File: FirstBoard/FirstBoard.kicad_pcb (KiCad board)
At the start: 2 copper layers, 82 x 122.1 mm, 26 parts, among them J0 Battery, J1 MPU0, J10 MPU9, J11 MPU10, J12 MPU11, J13 MPU12, J15 SD_CARD, J2 MPU1, J3 MPU3, J4 MPU3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

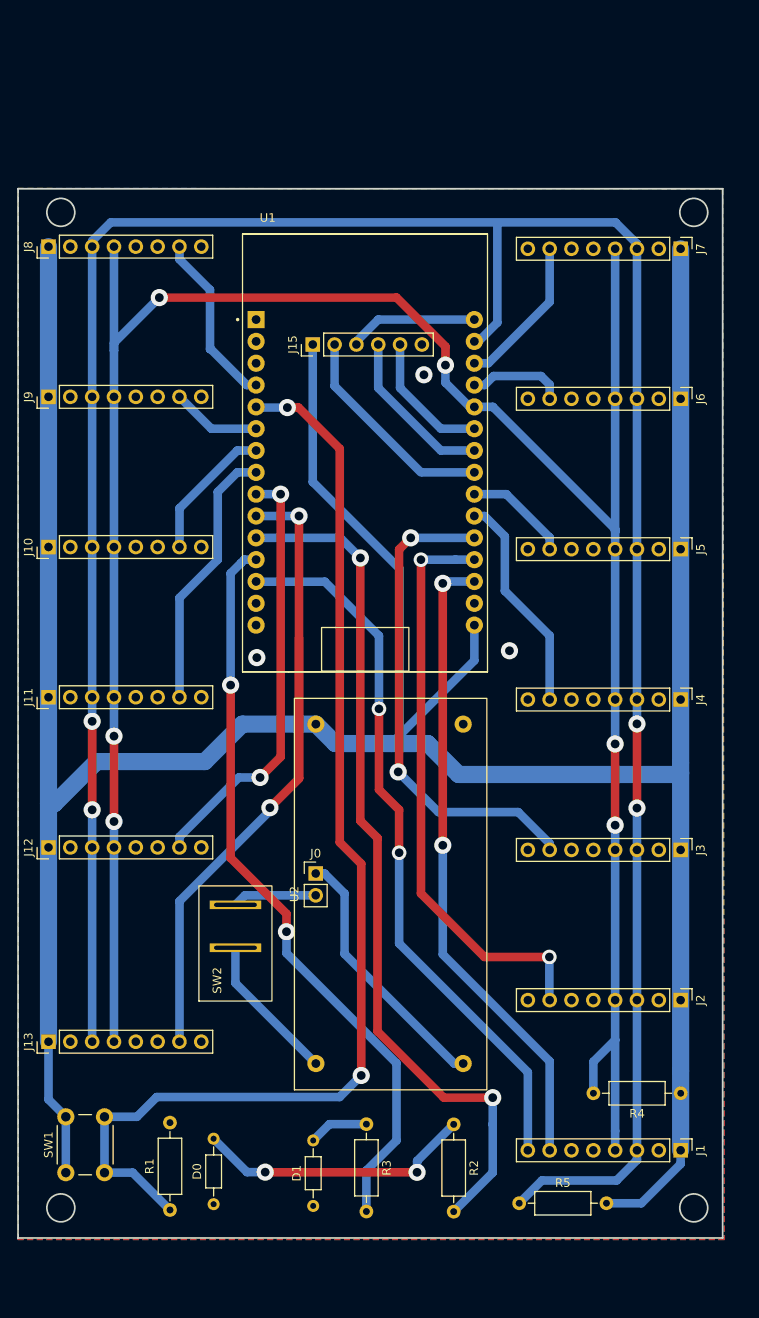
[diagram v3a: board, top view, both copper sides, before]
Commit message: Adjusted holes
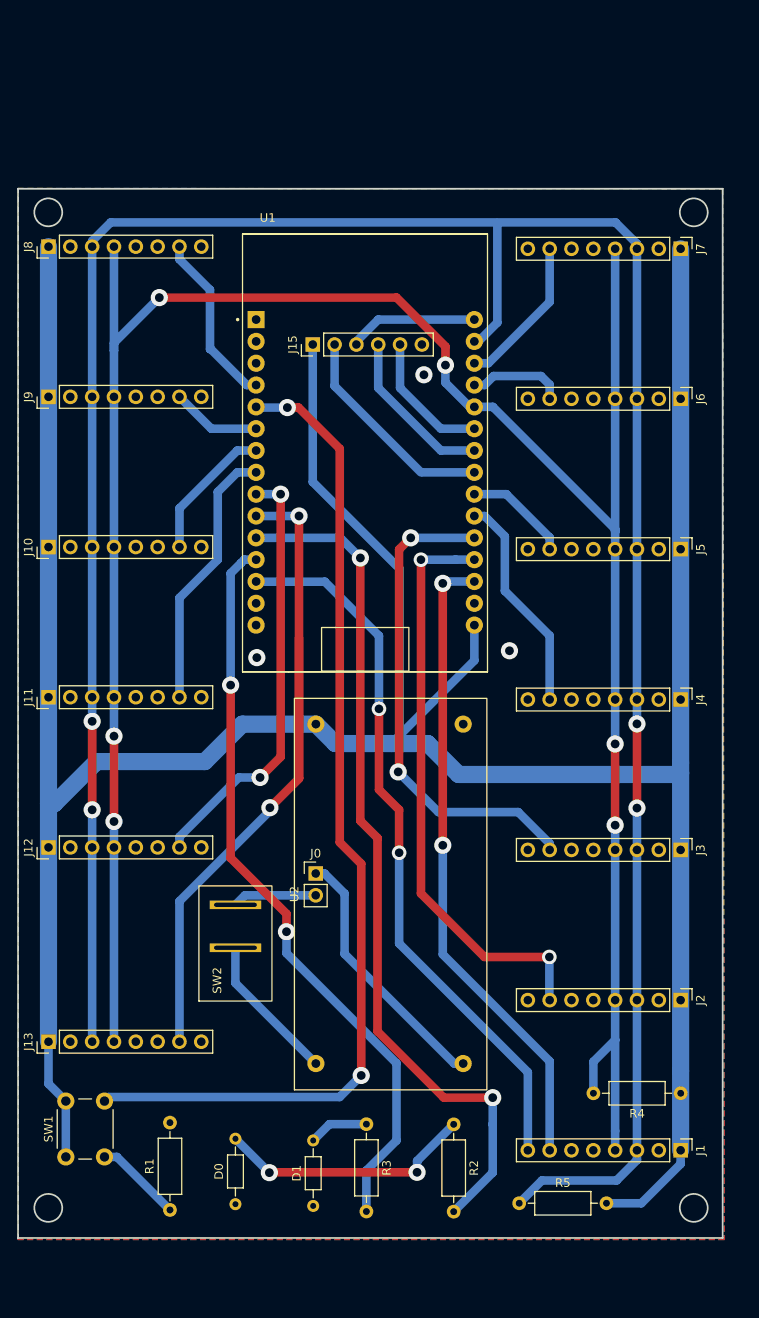
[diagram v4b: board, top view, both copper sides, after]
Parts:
- moved D0 2.54 mm to (66.5, 178.6)
- moved SW1 1.83 mm to (46.7, 173.1)
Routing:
- net Switch: track 133.5 -> 127.0 mm
- net Net-(D0-Pad2): track 32.6 -> 30.1 mm
- net 3v3: track 373.8 -> 372.0 mm
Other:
- outline, holes or cut-outs redrawn
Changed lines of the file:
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@@
   )
   (footprint "Button_Switch_THT:SW_PUSH_6mm_H5mm" (layer "F.Cu")
-    (at 46.74 174.9 90)
+    (at 46.74 173.07 90)
     (descr "tactile push button, 6x6mm e.g. PHAP33xx series, height=5mm")
     (tags "tact sw push 6mm")
@@
   )
   (footprint "Resistor_THT:R_Axial_DIN0204_L3.6mm_D1.6mm_P7.62mm_Horizontal" (layer "F.Cu")
-    (at 63.94 178.57 90)
+    (at 66.48 178.57 90)
     (descr "Resistor, Axial_DIN0204 series, Axial, Horizontal, pin pitch=7.62mm, 0.167W, length*diameter=3.6*1.6mm^2, http://cdn-reichelt.de/documents/datenblatt/B400/1_4W%23YAG.pdf")
     (tags "Resistor Axial_DIN0204 series Axial Horizontal pin pitch 7.62mm 0.167W length 3.6mm diameter 1.6mm")
@@
   (gr_line (start 89.34 61.719781) (end 89.34 79.800219)
     (stroke (width 0.2) (type solid)) (layer "B.SilkS"))
-  (gr_circle (center 46.16 179) (end 47.785 179)
+  (gr_circle (center 44.7 179) (end 46.325 179)
     (stroke (width 0.2) (type default)) (fill none) (layer "Edge.Cuts"))
   (gr_circle (center 119.82 179) (end 121.445 179)
@@
   (gr_rect (start 41.18 60.392616) (end 123.183126 182.5)
     (stroke (width 0.2) (type solid)) (fill none) (layer "Edge.Cuts"))
-  (gr_circle (center 46.16 63.14) (end 47.785 63.14)
+  (gr_circle (center 44.7 63.14) (end 46.325 63.14)
     (stroke (width 0.2) (type default)) (fill none) (layer "Edge.Cuts"))
   (dimension (type aligned) (layer "B.Cu")
@@
   (via (at 88.413456 82.044151) (size 2) (drill 1.02) (layers "F.Cu" "B.Cu") (free) (net 1))
   (via (at 68.97 114.96) (size 2) (drill 1.02) (layers "F.Cu" "B.Cu") (free) (net 1))
-  (segment (start 69.960777 174.86) (end 87.62 174.86) (width 1) (layer "F.Cu") (net 2))
-  (segment (start 69.941705 174.840928) (end 69.960777 174.86) (width 1) (layer "F.Cu") (net 2))
+  (segment (start 70.47 174.86) (end 87.62 174.86) (width 1) (layer "F.Cu") (net 2))
+  (segment (start 70.43 174.9) (end 70.47 174.86) (width 1) (layer "F.Cu") (net 2))
   (via (at 87.62 174.86) (size 2) (drill 1.02) (layers "F.Cu" "B.Cu") (net 2))
-  (via (at 69.941705 174.840928) (size 2) (drill 1.02) (layers "F.Cu" "B.Cu") (net 2))
+  (via (at 70.43 174.9) (size 2) (drill 1.02) (layers "F.Cu" "B.Cu") (net 2))
+  (segment (start 70.43 174.9) (end 66.48 170.95) (width 1) (layer "B.Cu") (net 2))
   (segment (start 87.62 174.86) (end 87.62 173.54) (width 1) (layer "B.Cu") (net 2))
   (segment (start 87.62 173.54) (end 91.88 169.28) (width 1) (layer "B.Cu") (net 2))
-  (segment (start 69.941705 174.840928) (end 67.830928 174.840928) (width 1) (layer "B.Cu") (net 2))
-  (segment (start 67.830928 174.840928) (end 63.94 170.95) (width 1) (layer "B.Cu") (net 2))
   (segment (start 81.72 169.26) (end 77.423827 169.26) (width 1) (layer "B.Cu") (net 3))
   (segment (start 77.423827 169.26) (end 75.529442 171.154385) (width 1) (layer "B.Cu") (net 3))
@@
   (segment (start 75.82 142.625) (end 67.588 142.625) (width 1) (layer "B.Cu") (net 5))
   (segment (start 44.725 131.955) (end 44.725 119.57) (width 2) (layer "B.Cu") (net 6))
-  (segment (start 44.725 166.385) (end 46.74 168.4) (width 1) (layer "B.Cu") (net 6))
   (segment (start 44.725 137.05) (end 44.725 159.66) (width 2) (layer "B.Cu") (net 6))
   (segment (start 85.57 124.01) (end 84.62 124.96) (width 1) (layer "B.Cu") (net 6))
   (segment (start 84.62 124.96) (end 78.097544 124.96) (width 2) (layer "B.Cu") (net 6))
+  (segment (start 46.734895 166.57) (end 44.725 164.560105) (width 1) (layer "B.Cu") (net 6))
   (segment (start 44.725 102.09) (end 44.725 84.61) (width 2) (layer "B.Cu") (net 6))
   (segment (start 118.29 127.19) (end 118.29 119.84) (width 2) (layer "B.Cu") (net 6))
+  (segment (start 44.725 164.560105) (end 44.725 159.66) (width 1) (layer "B.Cu") (net 6))
   (segment (start 118.29 67.38) (end 118.29 84.84) (width 2) (layer "B.Cu") (net 6))
   (segment (start 44.725 119.57) (end 44.725 102.09) (width 2) (layer "B.Cu") (net 6))
   (segment (start 44.725 137.05) (end 44.725 131.955) (width 2) (layer "B.Cu") (net 6))
   (segment (start 92.453001 128.56) (end 118.12 128.56) (width 2) (layer "B.Cu") (net 6))
-  (segment (start 46.74 168.4) (end 46.74 174.9) (width 1) (layer "B.Cu") (net 6))
   (segment (start 118.29 119.84) (end 118.29 102.34) (width 2) (layer "B.Cu") (net 6))
   (segment (start 118.29 163.08) (end 118.29 154.82) (width 2) (layer "B.Cu") (net 6))
@@
   (segment (start 84.62 124.96) (end 88.853001 124.96) (width 2) (layer "B.Cu") (net 6))
   (segment (start 67.277 122.703) (end 62.92 127.06) (width 2) (layer "B.Cu") (net 6))
-  (segment (start 44.725 159.66) (end 44.725 166.385) (width 1) (layer "B.Cu") (net 6))
   (segment (start 88.853001 124.96) (end 92.453001 128.56) (width 2) (layer "B.Cu") (net 6))
   (segment (start 85.57 104.61) (end 85.57 124.01) (width 1) (layer "B.Cu") (net 6))
@@
   (segment (start 118.29 137.34) (end 118.29 128.39) (width 2) (layer "B.Cu") (net 6))
   (segment (start 118.29 84.84) (end 118.29 102.34) (width 2) (layer "B.Cu") (net 6))
+  (segment (start 46.74 166.57) (end 46.734895 166.57) (width 1) (layer "B.Cu") (net 6))
   (segment (start 75.840544 122.703) (end 67.277 122.703) (width 2) (layer "B.Cu") (net 6))
+  (segment (start 46.74 173.07) (end 46.74 166.57) (width 1) (layer "B.Cu") (net 6))
   (segment (start 44.725 84.61) (end 44.725 67.13) (width 2) (layer "B.Cu") (net 6))
   (segment (start 75.478224 78.520748) (end 75.478224 94.518224) (width 1) (layer "B.Cu") (net 6))
@@
   (via (at 72.52 85.86) (size 2) (drill 1.02) (layers "F.Cu" "B.Cu") (net 41))
   (via (at 81.12 163.588576) (size 2) (drill 1.02) (layers "F.Cu" "B.Cu") (net 41))
-  (segment (start 51.24 174.9) (end 51.24 168.4) (width 1) (layer "B.Cu") (net 41))
+  (segment (start 51.24 166.57) (end 51.709336 166.100664) (width 1) (layer "B.Cu") (net 41))
   (segment (start 68.9646 85.86) (end 68.8848 85.7802) (width 1) (layer "B.Cu") (net 41))
-  (segment (start 55.02 168.4) (end 51.24 168.4) (width 1) (layer "B.Cu") (net 41))
-  (segment (start 81.12 163.588576) (end 78.607912 166.100664) (width 1) (layer "B.Cu") (net 41))
+  (segment (start 58.86 179.24) (end 52.69 173.07) (width 1) (layer "B.Cu") (net 41))
+  (segment (start 52.69 173.07) (end 51.24 173.07) (width 1) (layer "B.Cu") (net 41))
   (segment (start 72.52 85.86) (end 68.9646 85.86) (width 1) (layer "B.Cu") (net 41))
-  (segment (start 54.52 174.9) (end 58.86 179.24) (width 1) (layer "B.Cu") (net 41))
-  (segment (start 51.24 174.9) (end 54.52 174.9) (width 1) (layer "B.Cu") (net 41))
-  (segment (start 57.319336 166.100664) (end 55.02 168.4) (width 1) (layer "B.Cu") (net 41))
-  (segment (start 78.607912 166.100664) (end 57.319336 166.100664) (width 1) (layer "B.Cu") (net 41))
+  (segment (start 51.709336 166.100664) (end 78.607912 166.100664) (width 1) (layer "B.Cu") (net 41))
+  (segment (start 78.607912 166.100664) (end 81.12 163.588576) (width 1) (layer "B.Cu") (net 41))
   (segment (start 66.48 152.839456) (end 75.840544 162.2) (width 1) (layer "B.Cu") (net 72))
   (segment (start 66.48 148.73) (end 66.48 152.839456) (width 1) (layer "B.Cu") (net 72))

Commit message: Input-only pin changed
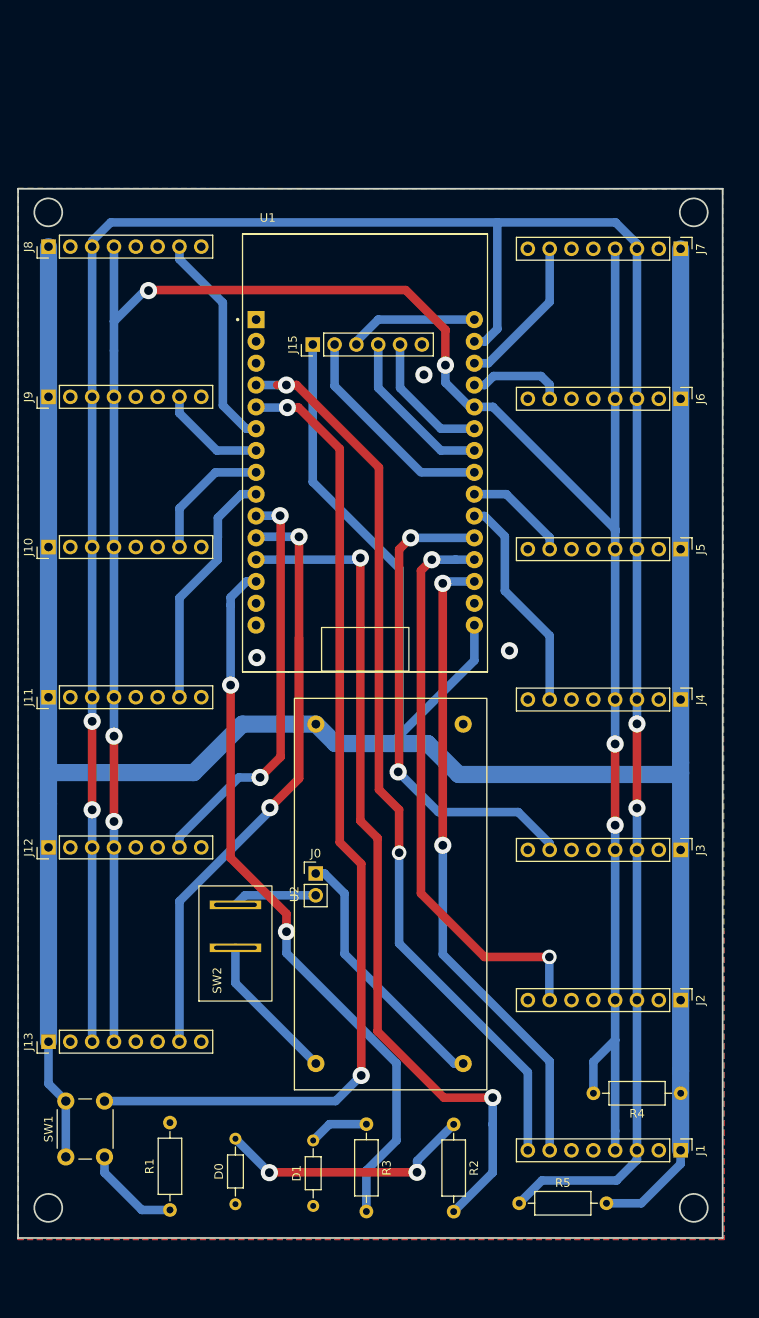
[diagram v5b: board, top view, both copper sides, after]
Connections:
- U1 pad 10: AD0_12 -> AD0_11
- U1 pad 11: LED_R -> AD0_12
- U1 pad 12: LED_G -> LED_R
- U1 pad 13: INT -> LED_G
- U1 pad 4: AD0_7 -> INT
- U1 pad 6: AD0_8 -> AD0_7
- U1 pad 7: AD0_9 -> AD0_8
- U1 pad 8: AD0_10 -> AD0_9
- U1 pad 9: AD0_11 -> AD0_10
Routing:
- net INT: track 84.0 -> 106.0 mm
- net AD0_7: track 20.5 -> 25.6 mm
- net AD0_10: track 31.1 -> 28.3 mm
- net LED_G: track 87.6 -> 85.0 mm
- net AD0_11: track 50.3 -> 47.8 mm
- net AD0_12: track 88.4 -> 86.0 mm
- net AD0_8: track 10.5 -> 12.6 mm
- net 3v3: track 372.0 -> 370.7 mm
- net Switch: track 127.0 -> 128.1 mm
- net AD0_9: track 16.2 -> 15.2 mm
- net LED_R: track 100.8 -> 99.9 mm
- net AD0_1: track 68.1 -> 67.4 mm
- net SCL: track 296.1 -> 296.6 mm
